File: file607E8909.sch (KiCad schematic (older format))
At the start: 8 parts, among them J1 Conn_01x06_Female, U3 INA4180A1IPWR, U5 254

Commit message: full schematic, version 1.0
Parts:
- C7: value C_Small -> 100nF; footprint (none) -> Capacitor_SMD:C_0603_1608Metric_Pad1.08x0.95mm_HandSolder
- J1: footprint (none) -> Connector_PinHeader_2.54mm:PinHeader_1x06_P2.54mm_Vertical
- R13: footprint (none) -> Resistor_SMD:R_0612_1632Metric_Pad1.18x3.40mm_HandSolder
- R15: value R_Small -> 0R2; footprint (none) -> Resistor_SMD:R_0612_1632Metric_Pad1.18x3.40mm_HandSolder
- R16: footprint (none) -> Resistor_SMD:R_1020_2550Metric_Pad1.33x5.20mm_HandSolder
- U3: footprint SOP65P640X120-14N -> EIPP:SOP65P640X120-14N
- U5: footprint MODULE_254 -> EIPP:MODULE_254
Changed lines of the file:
@@
 $Descr A4 11693 8268
 encoding utf-8
-Sheet 6 10
+Sheet 6 15
 Title ""
 Date ""
@@
 F 0 "U3" H 3050 3170 50  0000 C CNN
 F 1 "INA4180A1IPWR" H 3050 3079 50  0000 C CNN
-F 2 "SOP65P640X120-14N" H 3050 2300 50  0001 L BNN
+F 2 "EIPP:SOP65P640X120-14N" H 3050 2300 50  0001 L BNN
 F 3 "" H 3050 2300 50  0001 L BNN
 	1    3050 2300
@@
 F 0 "R13" V 1404 750 50  0000 C CNN
 F 1 "0R2" V 1495 750 50  0000 C CNN
-F 2 "" H 1600 750 50  0001 C CNN
+F 2 "Resistor_SMD:R_0612_1632Metric_Pad1.18x3.40mm_HandSolder" H 1600 750 50  0001 C CNN
 F 3 "~" H 1600 750 50  0001 C CNN
 	1    1600 750
@@
 P 1500 2800
 F 0 "C7" H 1592 2846 50  0000 L CNN
-F 1 "C_Small" H 1592 2755 50  0000 L CNN
-F 2 "" H 1500 2800 50  0001 C CNN
+F 1 "100nF" H 1592 2755 50  0000 L CNN
+F 2 "Capacitor_SMD:C_0603_1608Metric_Pad1.08x0.95mm_HandSolder" H 1500 2800 50  0001 C CNN
 F 3 "~" H 1500 2800 50  0001 C CNN
 	1    1500 2800
@@
 F 0 "R16" V 1354 1850 50  0000 C CNN
 F 1 "0R1" V 1445 1850 50  0000 C CNN
-F 2 "" H 1550 1850 50  0001 C CNN
+F 2 "Resistor_SMD:R_1020_2550Metric_Pad1.33x5.20mm_HandSolder" H 1550 1850 50  0001 C CNN
 F 3 "~" H 1550 1850 50  0001 C CNN
 	1    1550 1850
@@
 P 1350 2150
 F 0 "R15" V 1154 2150 50  0000 C CNN
-F 1 "R_Small" V 1245 2150 50  0000 C CNN
-F 2 "" H 1350 2150 50  0001 C CNN
+F 1 "0R2" V 1245 2150 50  0000 C CNN
+F 2 "Resistor_SMD:R_0612_1632Metric_Pad1.18x3.40mm_HandSolder" H 1350 2150 50  0001 C CNN
 F 3 "~" H 1350 2150 50  0001 C CNN
 	1    1350 2150
@@
 F 0 "U5" H 9450 3215 50  0000 C CNN
 F 1 "254" H 9450 3124 50  0000 C CNN
-F 2 "MODULE_254" H 9450 2550 50  0001 L BNN
+F 2 "EIPP:MODULE_254" H 9450 2550 50  0001 L BNN
 F 3 "" H 9450 2550 50  0001 L BNN
 F 4 "N/A" H 9450 2550 50  0001 L BNN "PARTREV"
@@
 F 0 "J1" H 2678 5526 50  0000 L CNN
 F 1 "Conn_01x06_Female" H 2678 5435 50  0000 L CNN
-F 2 "" H 2650 5550 50  0001 C CNN
+F 2 "Connector_PinHeader_2.54mm:PinHeader_1x06_P2.54mm_Vertical" H 2650 5550 50  0001 C CNN
 F 3 "~" H 2650 5550 50  0001 C CNN
 	1    2650 5550

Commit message: incomplete pcb
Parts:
- J1: footprint Connector_PinHeader_2.54mm:PinHeader_1x06_P2.54mm_Vertical -> Connector_PinSocket_2.54mm:PinSocket_1x06_P2.54mm_Vertical
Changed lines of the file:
@@
 	9950 2150 10150 2150
 NoConn ~ 10150 2150
+Text GLabel 2400 4150 0    50   Output ~ 0
+LOAD_3
+Wire Wire Line
+	2400 4150 2900 4150
+Wire Wire Line
+	2900 4250 2600 4250
+Wire Wire Line
+	2900 4450 2600 4450
+$Comp
+L power:GND #PWR066
+U 1 1 608EA451
+P 2600 4950
+F 0 "#PWR066" H 2600 4700 50  0001 C CNN
+F 1 "GND" H 2605 4777 50  0000 C CNN
+F 2 "" H 2600 4950 50  0001 C CNN
+F 3 "" H 2600 4950 50  0001 C CNN
+	1    2600 4950
+	1    0    0    -1
+$EndComp
+Text GLabel 2400 4350 0    50   Output ~ 0
+LOAD_2
+Text GLabel 2400 4550 0    50   Output ~ 0
+LOAD_1
+Wire Wire Line
+	2400 4550 2900 4550
 $Comp
 L Connector:Conn_01x06_Female J1
-U 1 1 608A75AE
-P 2650 5550
-F 0 "J1" H 2678 5526 50  0000 L CNN
-F 1 "Conn_01x06_Female" H 2678 5435 50  0000 L CNN
-F 2 "Connector_PinHeader_2.54mm:PinHeader_1x06_P2.54mm_Vertical" H 2650 5550 50  0001 C CNN
-F 3 "~" H 2650 5550 50  0001 C CNN
-	1    2650 5550
-	1    0    0    -1
-$EndComp
-$Comp
-L power:GND #PWR029
-U 1 1 608A8BC9
-P 2150 6000
-F 0 "#PWR029" H 2150 5750 50  0001 C CNN
-F 1 "GND" H 2155 5827 50  0000 C CNN
-F 2 "" H 2150 6000 50  0001 C CNN
-F 3 "" H 2150 6000 50  0001 C CNN
-	1    2150 6000
+U 1 1 6091EFB8
+P 3100 4350
+F 0 "J1" H 3128 4326 50  0000 L CNN
+F 1 "Conn_01x06_Female" H 3128 4235 50  0000 L CNN
+F 2 "Connector_PinSocket_2.54mm:PinSocket_1x06_P2.54mm_Vertical" H 3100 4350 50  0001 C CNN
+F 3 "~" H 3100 4350 50  0001 C CNN
+	1    3100 4350
 	1    0    0    -1
 $EndComp
 Wire Wire Line
-	2150 6000 2150 5850
+	2400 4350 2900 4350
 Wire Wire Line
-	2150 5850 2450 5850
+	2600 4250 2600 4450
 Wire Wire Line
-	2150 5850 2150 5650
+	2900 4650 2600 4650
 Wire Wire Line
-	2150 5650 2450 5650
-Connection ~ 2150 5850
+	2600 4650 2600 4950
 Wire Wire Line
-	2150 5650 2150 5450
-Wire Wire Line
-	2150 5450 2450 5450
-Connection ~ 2150 5650
-Text GLabel 1650 5750 0    50   Output ~ 0
-LOAD_1
-Text GLabel 1650 5550 0    50   Output ~ 0
-LOAD_2
-Text GLabel 1650 5350 0    50   Output ~ 0
-LOAD_3
-Wire Wire Line
-	1650 5350 2450 5350
-Wire Wire Line
-	2450 5550 1650 5550
-Wire Wire Line
-	1650 5750 2450 5750
+	2600 4650 2600 4450
+Connection ~ 2600 4650
+Connection ~ 2600 4450
 $EndSCHEMATC

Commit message: finished pcb v1
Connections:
- net A3: no longer names the net of A1.22 (A3)
- net A3: no longer U3.14 (OUT4)
- no-connect marks 22 -> 24
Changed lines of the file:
@@
 Wire Wire Line
 	3750 1900 3950 1900
-Wire Wire Line
-	3750 2000 3950 2000
 Text Label 3950 1800 0    50   ~ 0
 A1
 Text Label 3950 1900 0    50   ~ 0
 A2
-Text Label 3950 2000 0    50   ~ 0
-A3
 Text Label 7800 2700 0    50   ~ 0
 A0
@@
 Wire Wire Line
 	7600 2900 7800 2900
-Wire Wire Line
-	7600 3000 7800 3000
 Text Label 7800 2800 0    50   ~ 0
 A1
 Text Label 7800 2900 0    50   ~ 0
 A2
-Text Label 7800 3000 0    50   ~ 0
-A3
 NoConn ~ 7800 3100
 NoConn ~ 7800 3200
@@
 Connection ~ 2600 4650
 Connection ~ 2600 4450
+NoConn ~ 3750 2000
+NoConn ~ 7800 3000
+Wire Wire Line
+	7600 3000 7800 3000
 $EndSCHEMATC

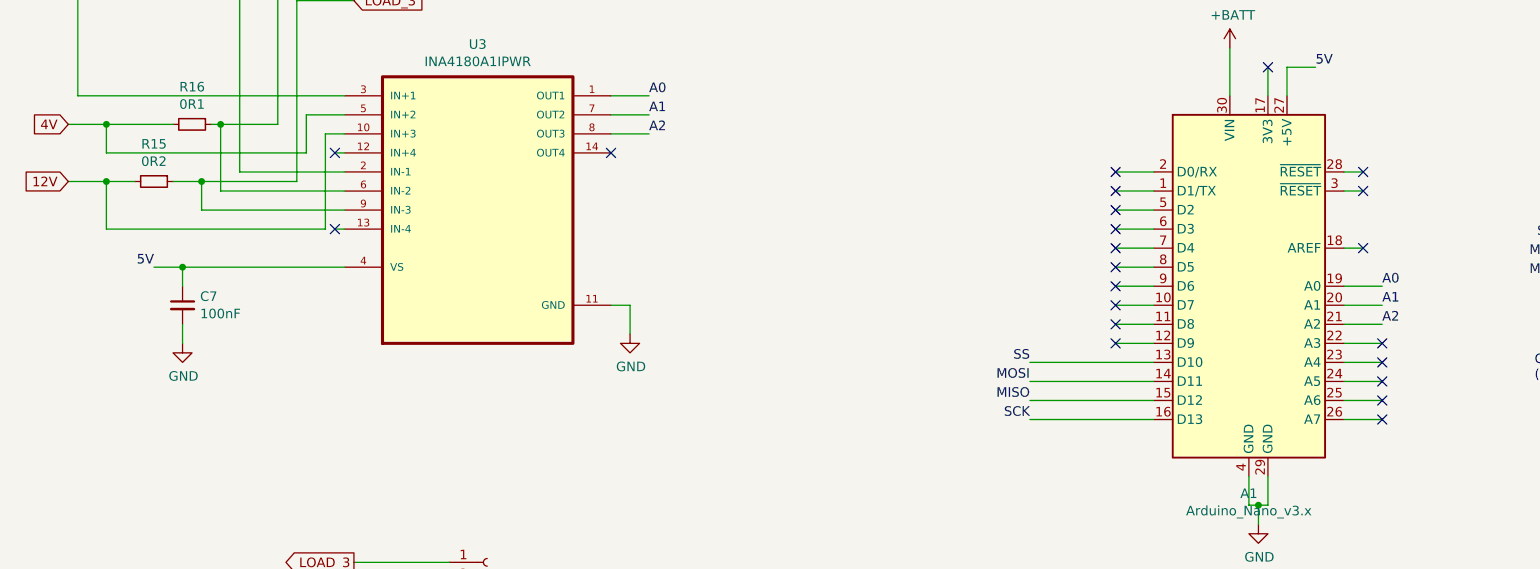
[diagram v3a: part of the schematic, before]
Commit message: changed unavailable parts, added overall consumed current measuring
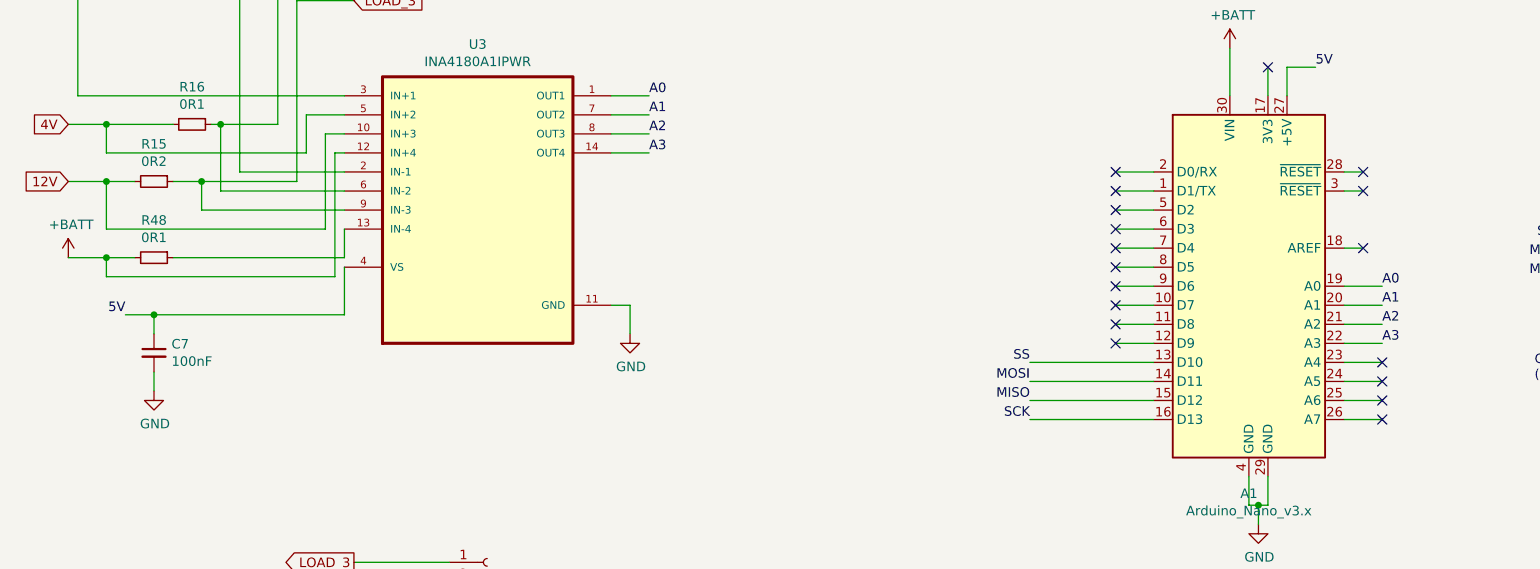
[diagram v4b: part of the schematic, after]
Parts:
- added R48: 0R1, Resistor_SMD:R_1020_2550Metric_Pad1.33x5.20mm_HandSolder, symbol Device:R_Small
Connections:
- net +BATT: now also U3.12 (IN+4), R48.2
- net A3: now reaches A1.22 (A3)
- net A3: now also U3.14 (OUT4)
- net at U3.13 (IN-4): now also R48.1
- no-connect marks 24 -> 20
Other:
- moved on the sheet: C7
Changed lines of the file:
@@
 Wire Wire Line
 	950  750  1500 750
-Wire Wire Line
-	2350 2600 1500 2600
 $Comp
 L Device:C_Small C7
 U 1 1 607F8D15
-P 1500 2800
-F 0 "C7" H 1592 2846 50  0000 L CNN
-F 1 "100nF" H 1592 2755 50  0000 L CNN
-F 2 "Capacitor_SMD:C_0603_1608Metric_Pad1.08x0.95mm_HandSolder" H 1500 2800 50  0001 C CNN
-F 3 "~" H 1500 2800 50  0001 C CNN
-	1    1500 2800
-	1    0    0    -1
-$EndComp
-Wire Wire Line
-	1500 2600 1500 2700
-Connection ~ 1500 2600
-Wire Wire Line
-	1500 2600 1350 2600
+P 1350 3050
+F 0 "C7" H 1442 3096 50  0000 L CNN
+F 1 "100nF" H 1442 3005 50  0000 L CNN
+F 2 "Capacitor_SMD:C_0603_1608Metric_Pad1.08x0.95mm_HandSolder" H 1350 3050 50  0001 C CNN
+F 3 "~" H 1350 3050 50  0001 C CNN
+	1    1350 3050
+	1    0    0    -1
+$EndComp
+Wire Wire Line
+	1350 2850 1350 2950
+Connection ~ 1350 2850
+Wire Wire Line
+	1350 2850 1200 2850
 $Comp
 L power:GND #PWR06
 U 1 1 607F9AA8
-P 1500 3000
-F 0 "#PWR06" H 1500 2750 50  0001 C CNN
-F 1 "GND" H 1505 2827 50  0000 C CNN
-F 2 "" H 1500 3000 50  0001 C CNN
-F 3 "" H 1500 3000 50  0001 C CNN
-	1    1500 3000
-	1    0    0    -1
-$EndComp
-Wire Wire Line
-	1500 2900 1500 3000
+P 1350 3250
+F 0 "#PWR06" H 1350 3000 50  0001 C CNN
+F 1 "GND" H 1355 3077 50  0000 C CNN
+F 2 "" H 1350 3250 50  0001 C CNN
+F 3 "" H 1350 3250 50  0001 C CNN
+	1    1350 3250
+	1    0    0    -1
+$EndComp
+Wire Wire Line
+	1350 3150 1350 3250
 Wire Wire Line
 	3750 2800 3850 2800
@@
 NoConn ~ 7700 2200
 NoConn ~ 7700 2500
-Wire Wire Line
-	2350 2000 2300 2000
-Wire Wire Line
-	2350 2400 2300 2400
-NoConn ~ 2300 2000
-NoConn ~ 2300 2400
-Text Label 1350 2600 2    50   ~ 0
+Text Label 1200 2850 2    50   ~ 0
 5V
 $Comp
@@
 Connection ~ 2600 4650
 Connection ~ 2600 4450
-NoConn ~ 3750 2000
-NoConn ~ 7800 3000
 Wire Wire Line
 	7600 3000 7800 3000
+$Comp
+L Device:R_Small R48
+U 1 1 609734E1
+P 1350 2550
+F 0 "R48" V 1154 2550 50  0000 C CNN
+F 1 "0R1" V 1245 2550 50  0000 C CNN
+F 2 "Resistor_SMD:R_1020_2550Metric_Pad1.33x5.20mm_HandSolder" H 1350 2550 50  0001 C CNN
+F 3 "~" H 1350 2550 50  0001 C CNN
+	1    1350 2550
+	0    1    1    0
+$EndComp
+Wire Wire Line
+	2350 2850 2350 2600
+Wire Wire Line
+	1350 2850 2350 2850
+$Comp
+L power:+BATT #PWR067
+U 1 1 6097FBBD
+P 900 2550
+F 0 "#PWR067" H 900 2400 50  0001 C CNN
+F 1 "+BATT" H 915 2723 50  0000 C CNN
+F 2 "" H 900 2550 50  0001 C CNN
+F 3 "" H 900 2550 50  0001 C CNN
+	1    900  2550
+	1    0    0    -1
+$EndComp
+Wire Wire Line
+	2350 2550 2350 2400
+Wire Wire Line
+	1450 2550 2350 2550
+Wire Wire Line
+	1100 2550 1100 2650
+Wire Wire Line
+	2300 2000 2350 2000
+Wire Wire Line
+	1100 2650 2300 2650
+Connection ~ 1100 2550
+Wire Wire Line
+	1100 2550 1250 2550
+Wire Wire Line
+	900  2550 1100 2550
+Wire Wire Line
+	2300 2650 2300 2000
+Wire Wire Line
+	3750 2000 3950 2000
+Text Label 3950 2000 0    50   ~ 0
+A3
+Text Label 7800 3000 0    50   ~ 0
+A3
 $EndSCHEMATC

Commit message: finished pcb v2
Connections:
- net labels added: +8V
- wire segments 103 -> 110
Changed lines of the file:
@@
 $EndComp
-Wire Wire Line
-	1350 3150 1350 3250
 Wire Wire Line
 	3750 2800 3850 2800
@@
 Wire Wire Line
 	1100 2000 2150 2000
-Wire Wire Line
-	2150 2000 2150 1800
 Wire Wire Line
 	2150 1800 2350 1800
@@
 Wire Wire Line
 	1350 2850 2350 2850
-$Comp
-L power:+BATT #PWR067
-U 1 1 6097FBBD
-P 900 2550
-F 0 "#PWR067" H 900 2400 50  0001 C CNN
-F 1 "+BATT" H 915 2723 50  0000 C CNN
-F 2 "" H 900 2550 50  0001 C CNN
-F 3 "" H 900 2550 50  0001 C CNN
-	1    900  2550
-	1    0    0    -1
-$EndComp
 Wire Wire Line
 	2350 2550 2350 2400
-Wire Wire Line
-	1450 2550 2350 2550
 Wire Wire Line
 	1100 2550 1100 2650
@@
 Text Label 7800 3000 0    50   ~ 0
 A3
+Wire Wire Line
+	2150 2000 2150 1800
+Wire Wire Line
+	1450 2550 1950 2550
+Connection ~ 1950 2550
+Wire Wire Line
+	1950 2550 2350 2550
+Wire Wire Line
+	2600 1400 2300 1400
+Wire Wire Line
+	1950 1400 1950 2550
+$Comp
+L power:+8V #PWR?
+U 1 1 609E1C5B
+P 900 2550
+AR Path="/6080506F/609E1C5B" Ref="#PWR?"  Part="1"
+AR Path="/607E890A/609E1C5B" Ref="#PWR0115"  Part="1"
+F 0 "#PWR0115" H 900 2400 50  0001 C CNN
+F 1 "+8V" V 915 2678 50  0000 L CNN
+F 2 "" H 900 2550 50  0001 C CNN
+F 3 "" H 900 2550 50  0001 C CNN
+	1    900  2550
+	1    0    0    -1
+$EndComp
+$Comp
+L power:+BATT #PWR?
+U 1 1 609E870F
+P 2600 1400
+AR Path="/607D64D2/607F1961/609E870F" Ref="#PWR?"  Part="1"
+AR Path="/608CA2DC/608CBCF1/609E870F" Ref="#PWR?"  Part="1"
+AR Path="/60925CA4/60926DAB/609E870F" Ref="#PWR?"  Part="1"
+AR Path="/60925CA4/6094117B/609E870F" Ref="#PWR?"  Part="1"
+AR Path="/60925CA4/60835FC2/609E870F" Ref="#PWR?"  Part="1"
+AR Path="/607E890A/609E870F" Ref="#PWR0113"  Part="1"
+F 0 "#PWR0113" H 2600 1250 50  0001 C CNN
+F 1 "+BATT" H 2615 1573 50  0000 C CNN
+F 2 "" H 2600 1400 50  0001 C CNN
+F 3 "" H 2600 1400 50  0001 C CNN
+	1    2600 1400
+	0    1    1    0
+$EndComp
+Wire Wire Line
+	1350 3150 1350 3200
+$Comp
+L power:PWR_FLAG #FLG0103
+U 1 1 609FE167
+P 2300 1300
+F 0 "#FLG0103" H 2300 1375 50  0001 C CNN
+F 1 "PWR_FLAG" H 2300 1473 50  0000 C CNN
+F 2 "" H 2300 1300 50  0001 C CNN
+F 3 "~" H 2300 1300 50  0001 C CNN
+	1    2300 1300
+	1    0    0    -1
+$EndComp
+Wire Wire Line
+	2300 1300 2300 1400
+Connection ~ 2300 1400
+Wire Wire Line
+	2300 1400 1950 1400
+$Comp
+L power:PWR_FLAG #FLG0104
+U 1 1 60A03053
+P 1100 3200
+F 0 "#FLG0104" H 1100 3275 50  0001 C CNN
+F 1 "PWR_FLAG" V 1100 3327 50  0000 L CNN
+F 2 "" H 1100 3200 50  0001 C CNN
+F 3 "~" H 1100 3200 50  0001 C CNN
+	1    1100 3200
+	0    -1   -1   0
+$EndComp
+Wire Wire Line
+	1100 3200 1350 3200
+Connection ~ 1350 3200
+Wire Wire Line
+	1350 3200 1350 3250
 $EndSCHEMATC
